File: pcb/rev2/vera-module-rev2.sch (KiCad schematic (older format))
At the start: 119 parts, among them J1 Bus, J2 Prog, J3 SD_Card, J4 Composite, J5 VGA, J6 Conn_01x04, J7 Conn_01x02, J8 RS232, J9 S-video, U1 ICE40UP5K-SG48ITR50, U10 MIC5504-3.3YM5, U11 THS7314D, U12 MAX3221CPWR, U2 74AHC00PW, U3 SN74CBTD3861PWR, U4 74AHC1G14GW,125, U5 74LVC4245APW, U6 WM8524CGEDT, U7 W25Q16JVSNIQ, U8 74AHC1G14GW,125, U9 AP3417CKTR-G1, X1 SG5032CAN_25.000000M-TJGA3

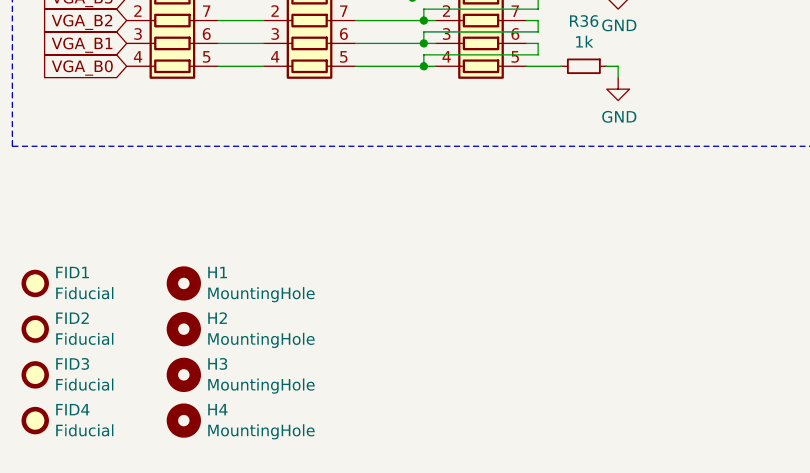
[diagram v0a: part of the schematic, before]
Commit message: Rev2 PCB: added X16 logo.
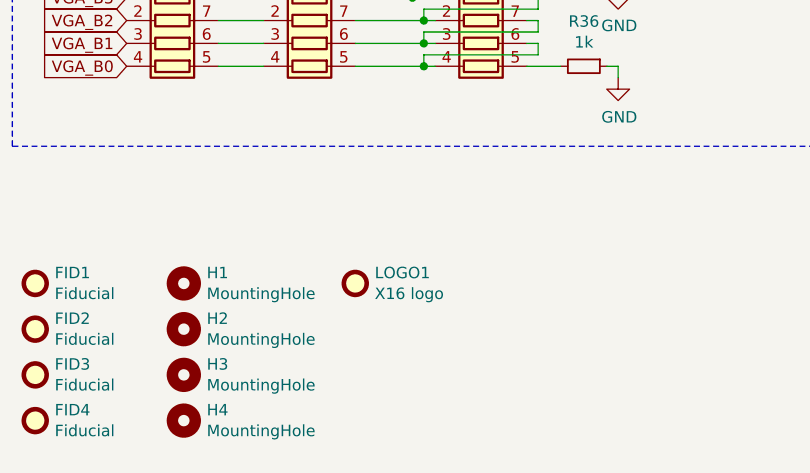
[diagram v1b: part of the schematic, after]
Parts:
- added LOGO1: X16 logo, vera-module:x16logo, symbol Mechanical:Fiducial
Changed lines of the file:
@@
 NoConn ~ 12950 8700
 NoConn ~ 12450 8700
+$Comp
+L Mechanical:Fiducial LOGO1
+U 1 1 5E4B2D01
+P 4250 10350
+F 0 "LOGO1" H 4335 10396 50  0000 L CNN
+F 1 "X16 logo" H 4335 10305 50  0000 L CNN
+F 2 "vera-module:x16logo" H 4250 10350 50  0001 C CNN
+F 3 "~" H 4250 10350 50  0001 C CNN
+	1    4250 10350
+	1    0    0    -1
+$EndComp
 $EndSCHEMATC
